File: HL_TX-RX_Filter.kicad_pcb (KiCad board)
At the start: 2 copper layers, 100 x 100 mm, 201 parts, among them J1 CNR1, J10 To Rx in, J2 CNR3, J3 Antenna, J4 CNR2, J5 CNR4, J6 From Tx, J7 ICSP, J8 SCL SDA, J9 Input1, Q1 2N7002, Q2 2N7002, Q3 2N7002, Q4 2N7002, Q5 2N7002, Q6 2N7002, Q7 2N7002, Q8 2N7002, U1 ATMEGA328-AU, U10 PE4259, U11 PE4259, U12 PE4259, U2 PE4259, U3 PE4259, U4 PE4259, U5 PE4259, U6 PE4259, U7 PE4259, U8 PE4259, U9 PE4259

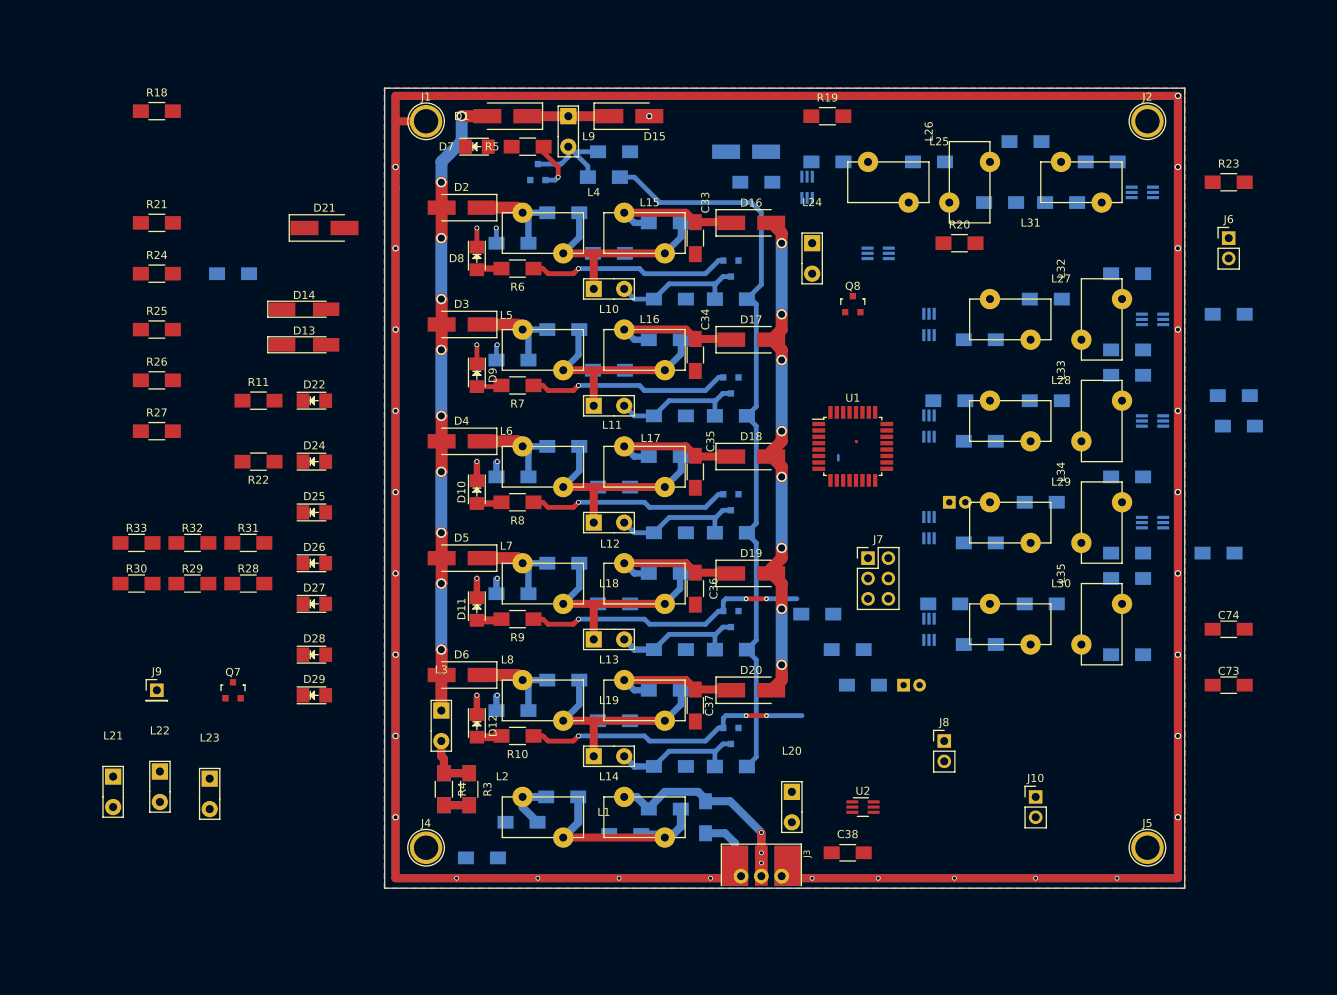
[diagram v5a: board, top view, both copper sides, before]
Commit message: Working on laying out Receive Filters
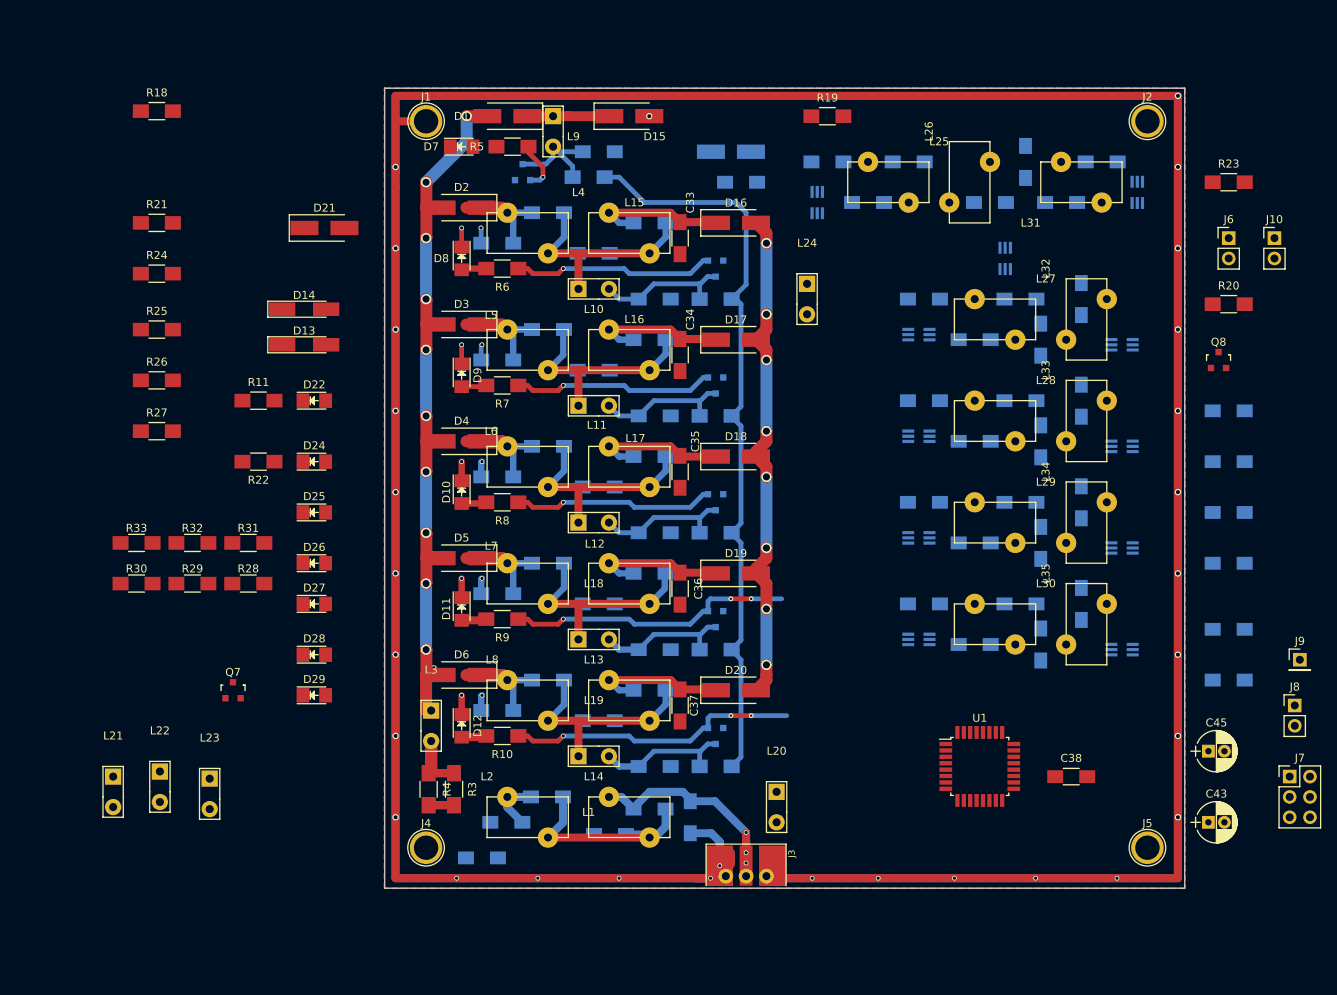
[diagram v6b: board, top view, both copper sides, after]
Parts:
- C43, C45: moved to F.Cu
- C73, C74, U2: moved to B.Cu
- moved J9 142.9 mm to (239.4, 131.4)
- moved C69 111.1 mm to (207.0, 129.5), turned to 90 degrees
- moved J10 76.0 mm to (236.2, 78.7)
- moved U2 75.8 mm to (179.1, 74.3), turned to 270 degrees
- moved C70 66.8 mm to (214.6, 69.2)
- moved C40 66.6 mm to (230.5, 113.0)
- moved U8 60.5 mm to (219.1, 73.0)
- moved J7 59.4 mm to (238.1, 146.1)
- moved C47 53.4 mm to (230.5, 119.4)
- moved C42 53.0 mm to (230.5, 106.7)
- moved C60 50.5 mm to (205.1, 69.2), turned to 270 degrees
- moved C50 48.4 mm to (190.5, 69.2), turned to 0 degrees
- moved C61 46.4 mm to (204.5, 86.4)
- moved Q8 46.3 mm to (229.2, 94.0)
- moved C41 45.7 mm to (230.5, 134.0)
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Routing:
- net GND: track 804.5 -> 807.5 mm, vias 38 -> 39
- net (no net): track 0.66 -> 0.00 mm
- net Net-(C48-Pad1): track 0.00 -> 0.58 mm
- net Net-(C40-Pad1): track 63.5 -> 62.9 mm

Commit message: Wiring of Rx filters
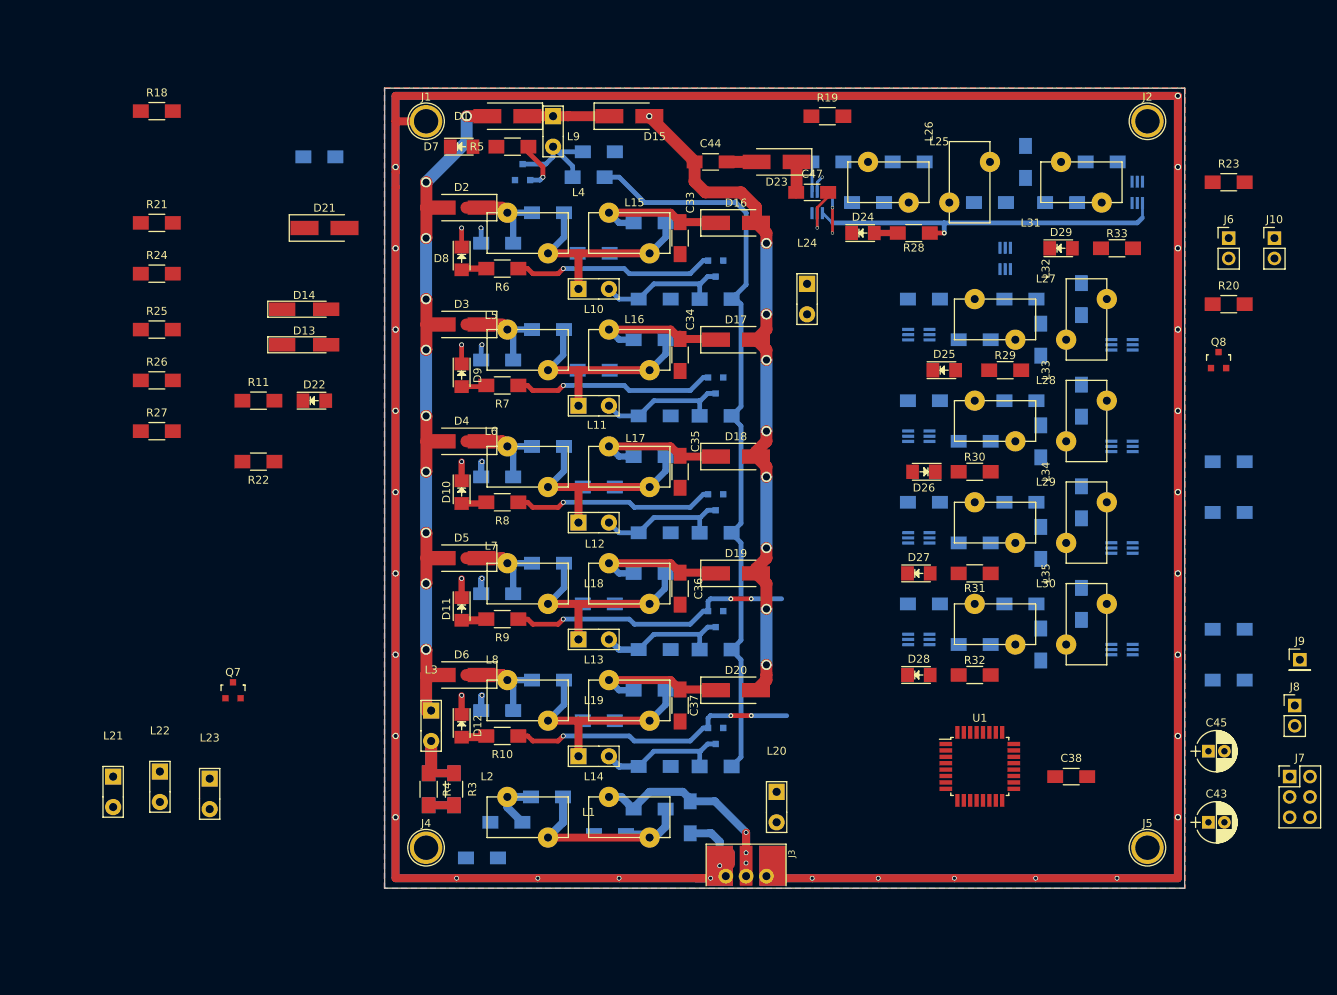
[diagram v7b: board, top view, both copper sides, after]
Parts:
- C44, C47, D23: moved to F.Cu
- moved R33 128.0 mm to (216.5, 80.0)
- moved D29 108.8 mm to (209.6, 80.0)
- moved R30 105.7 mm to (198.8, 108.0)
- moved R29 105.0 mm to (202.6, 95.2)
- moved R32 99.2 mm to (198.8, 133.3)
- moved R28 94.0 mm to (191.1, 78.1), turned to 180 degrees
- moved R31 90.9 mm to (198.8, 120.7), turned to 180 degrees
- moved D25 80.7 mm to (194.9, 95.2)
- moved D26 77.1 mm to (192.4, 108.0), turned to 180 degrees
- moved D27 75.7 mm to (191.8, 120.7)
- moved D28 75.6 mm to (191.8, 133.3)
- moved D24 74.3 mm to (184.8, 78.1)
- moved C44 71.9 mm to (165.7, 69.2)
- moved C47 69.7 mm to (178.4, 73.0)
- moved C39 52.8 mm to (116.8, 68.6)
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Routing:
- net /R1: track 0.00 -> 45.7 mm, vias 0 -> 1
- net Net-(C40-Pad1): track 62.9 -> 84.4 mm
- net Net-(C47-Pad2): track 0.00 -> 6.86 mm, vias 0 -> 1
- net Net-(U2-Pad3): track 0.00 -> 5.99 mm, vias 0 -> 2
- net Net-(C47-Pad1): track 0.00 -> 3.83 mm
- net Net-(C44-Pad2): track 0.00 -> 3.75 mm
- net Net-(C48-Pad1): track 0.58 -> 3.78 mm
- net Net-(D24-Pad2): track 0.00 -> 2.93 mm
- net GND: track 807.5 -> 809.6 mm, vias 39 -> 40

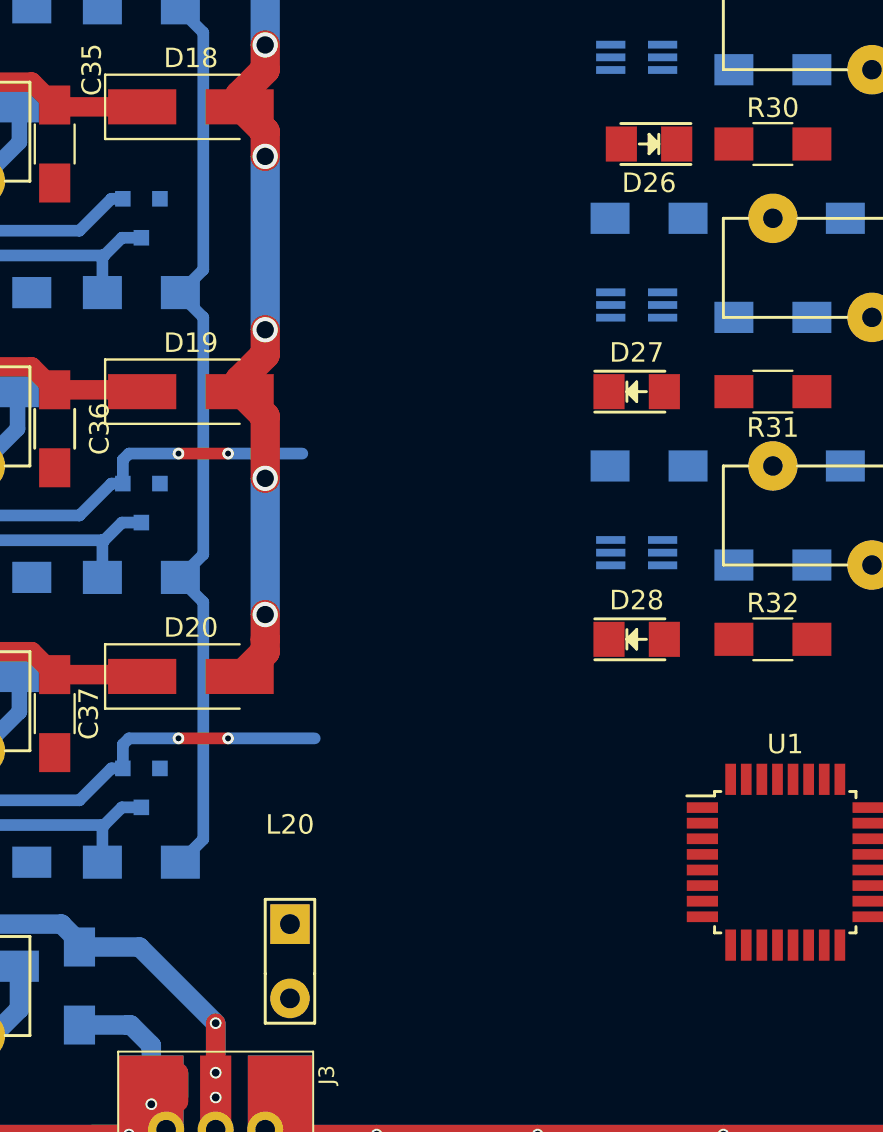
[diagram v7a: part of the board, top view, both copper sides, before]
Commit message: Laying tracks for Tx switching
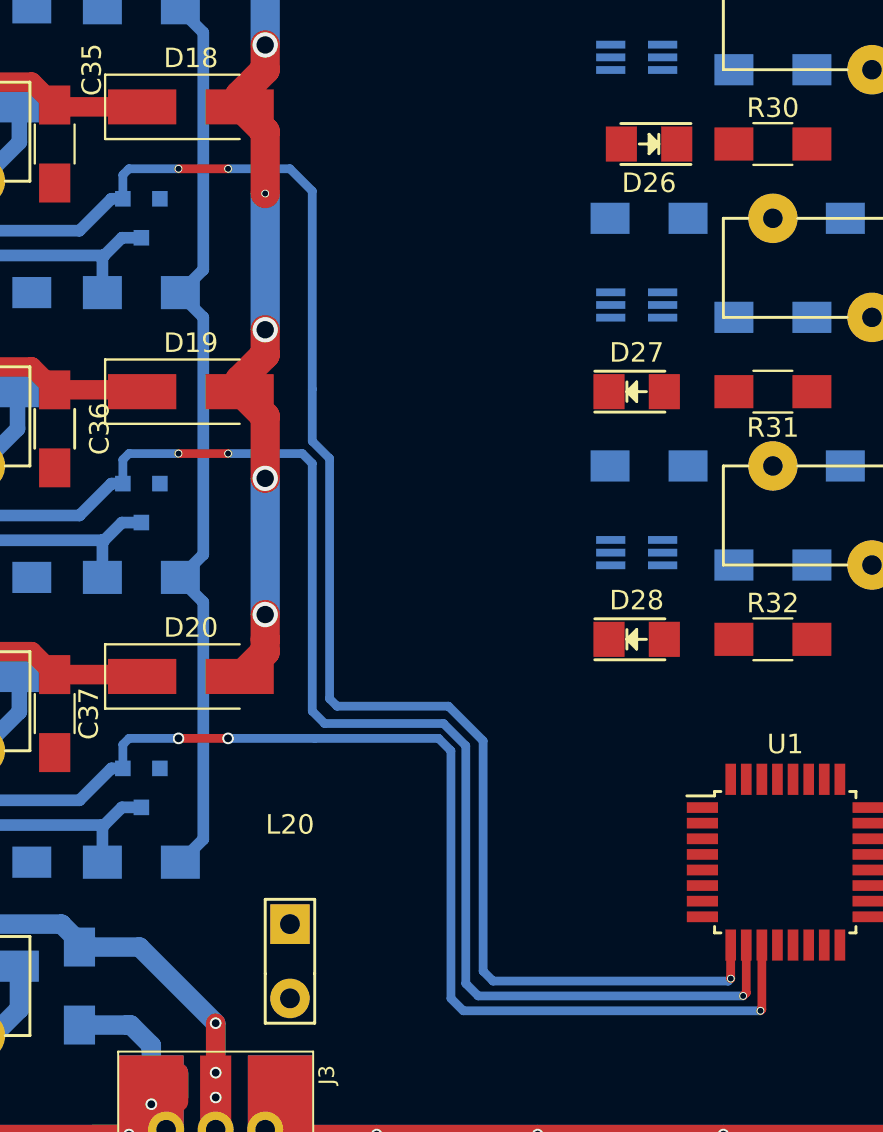
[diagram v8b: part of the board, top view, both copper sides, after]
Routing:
- net /T40: track 25.2 -> 98.4 mm, vias 1 -> 4
- net /T80: track 35.7 -> 87.1 mm, vias 3 -> 4
- net /T160: track 36.4 -> 75.9 mm, vias 3 -> 4
